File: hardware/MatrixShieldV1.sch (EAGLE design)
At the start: 10 parts, among them J1 CON_HEADER_2X08-PTH-SHROUDED, J4 1X2-5.0

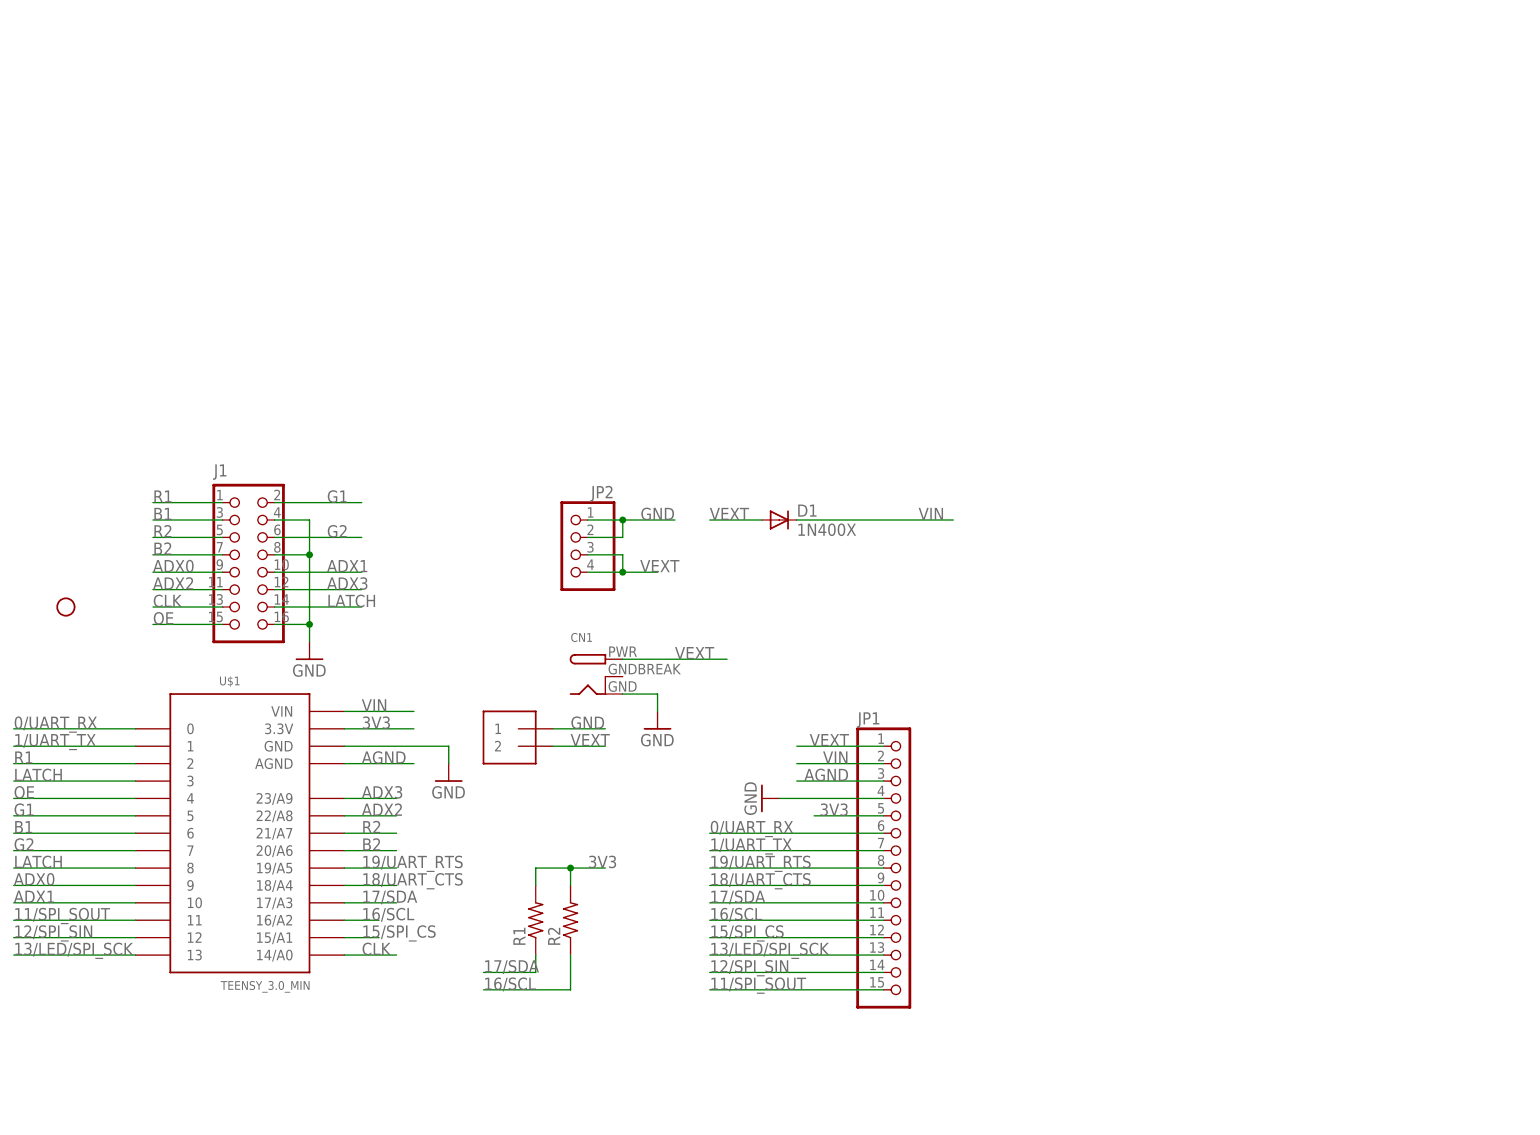
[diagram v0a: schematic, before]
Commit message: Cleaned up schematic Added license to schematic and board
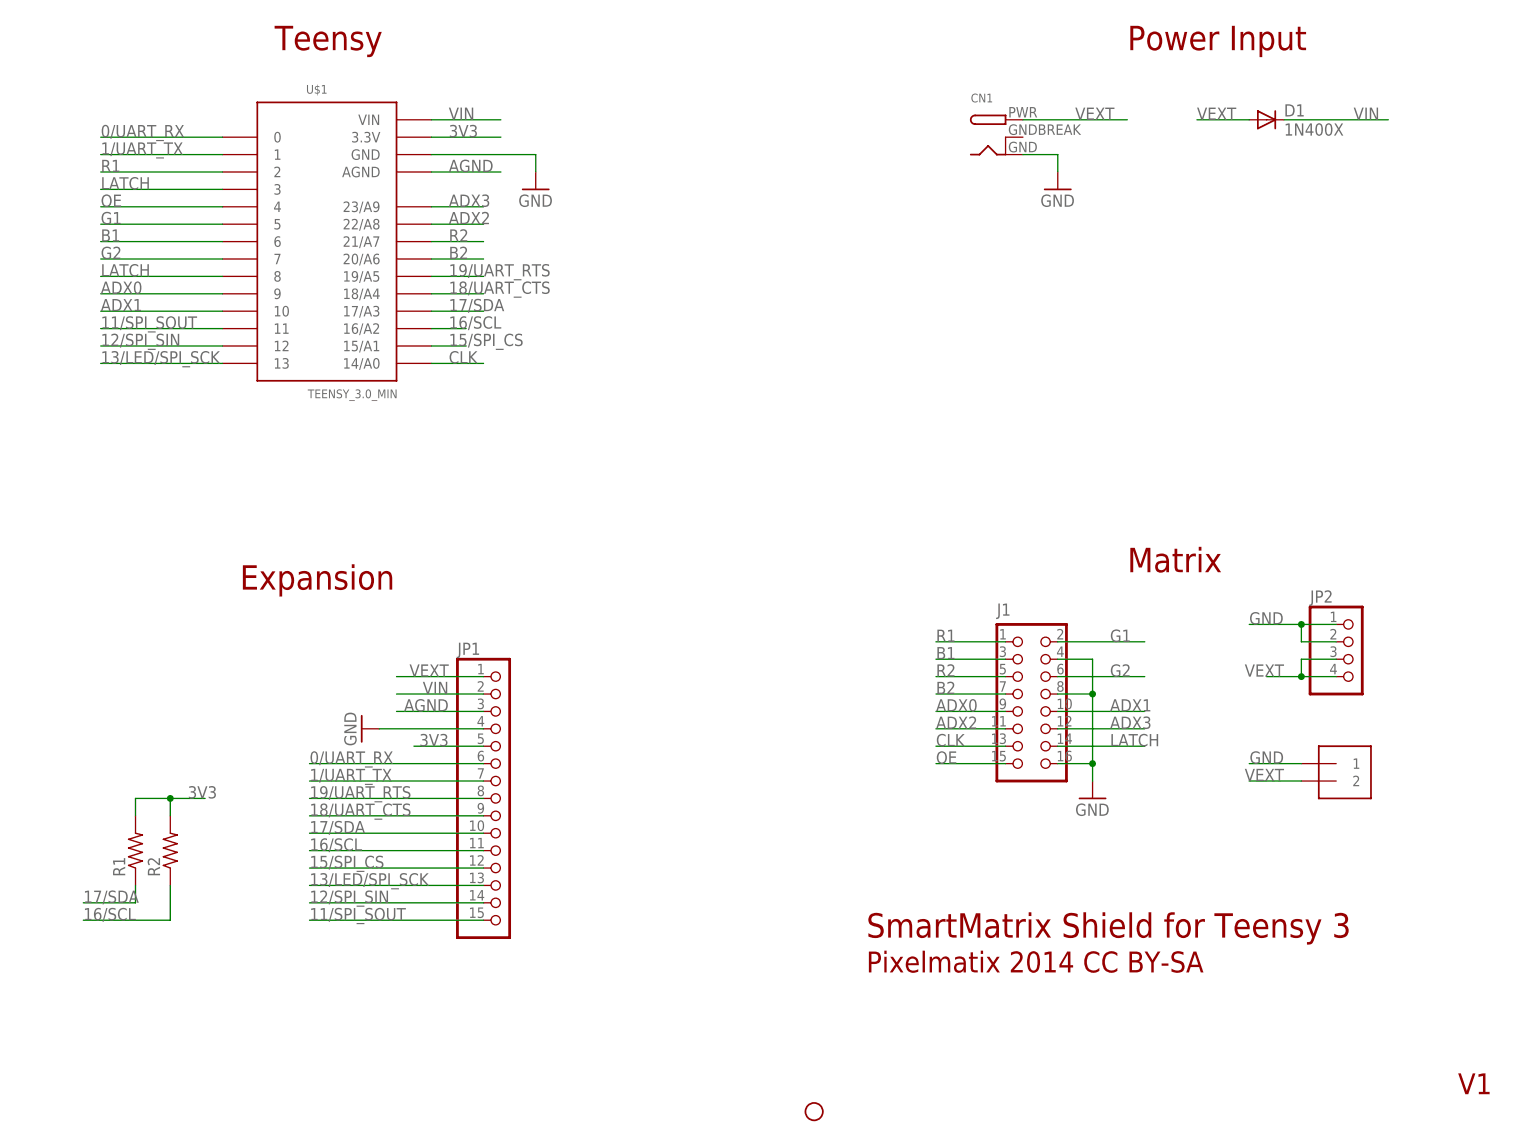
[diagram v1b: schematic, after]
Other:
- note added: "Expansion"
- note added: "Matrix"
- note added: "Pixelmatix 2014 CC BY-SA"
- note added: "Power Input"
- note added: "SmartMatrix Shield for Teensy 3"
- note added: "Teensy"
- note added: "V1"
- moved on the sheet: CN1, D1, J1, JP1, JP2, R1, R2, U$1
